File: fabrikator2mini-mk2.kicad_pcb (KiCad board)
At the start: 2 copper layers, 100 x 100 mm, 118 parts, among them CON1 Micro_SD_Card, J1 USB_OTG, J10 END_X/ESP, J11 MT_Y, J12 Conn_01x12, J13 Z, J14 MT_Z, J15 B, J16 BTN1, J17 Fan1, J2 RESET, J3 PWR_IN, J4 B, J5 I2C, J6 SWD, J7 SPI, J8 Fan2, J9 MT_X, P16 SW_DIP, P17 SW_DIP, P18 SW_DIP, P19 SW_DIP, Q1 PSMN2R4-30MLD, Q2 PSMN2R4-30MLD, Q3 PSMN2R4-30MLD, Q4 PSMN2R4-30MLD, Q5 Si7145DP, U1 bluepill, U2 CPDT6-5V4, U3 CPDT6-5V4, U4 4988, U5 4988, U6 4988, U7 4988, U9 TS30011

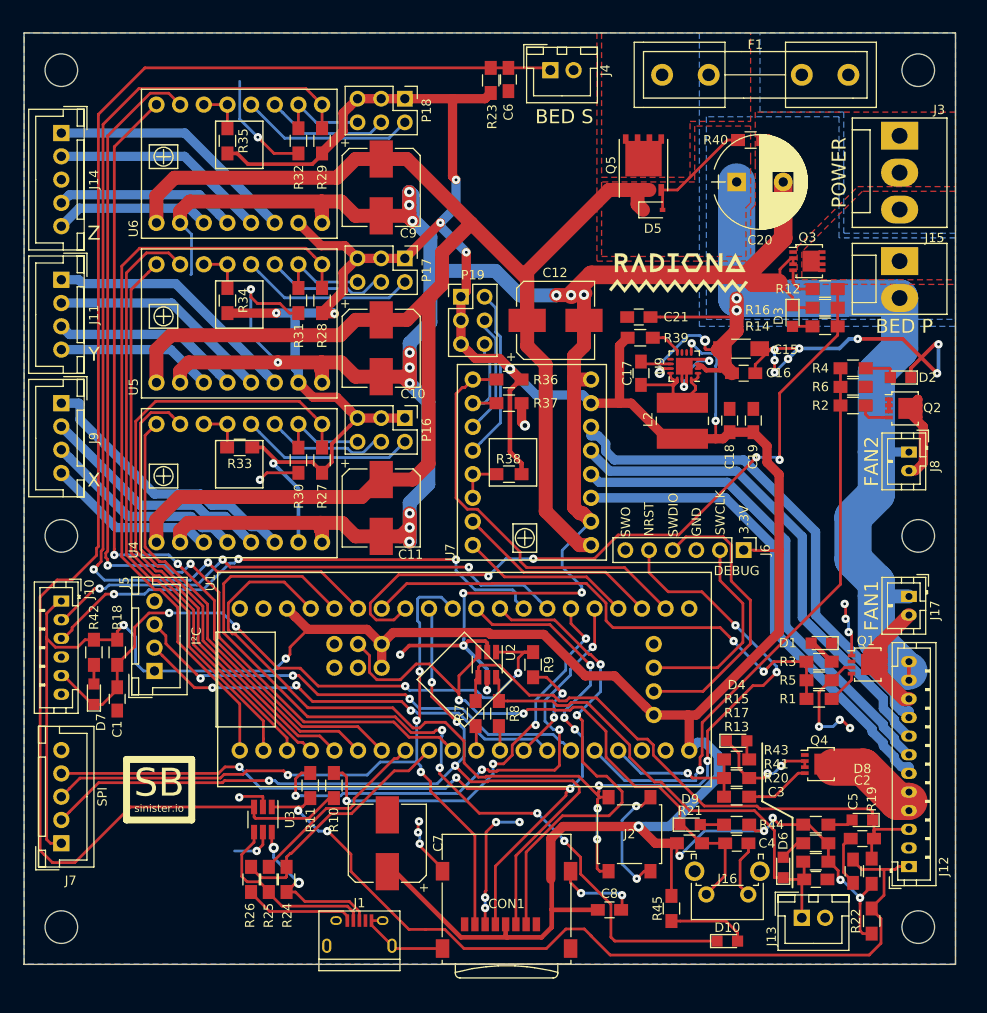
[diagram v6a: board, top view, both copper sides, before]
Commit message: fixed modules after switch to kicad 5
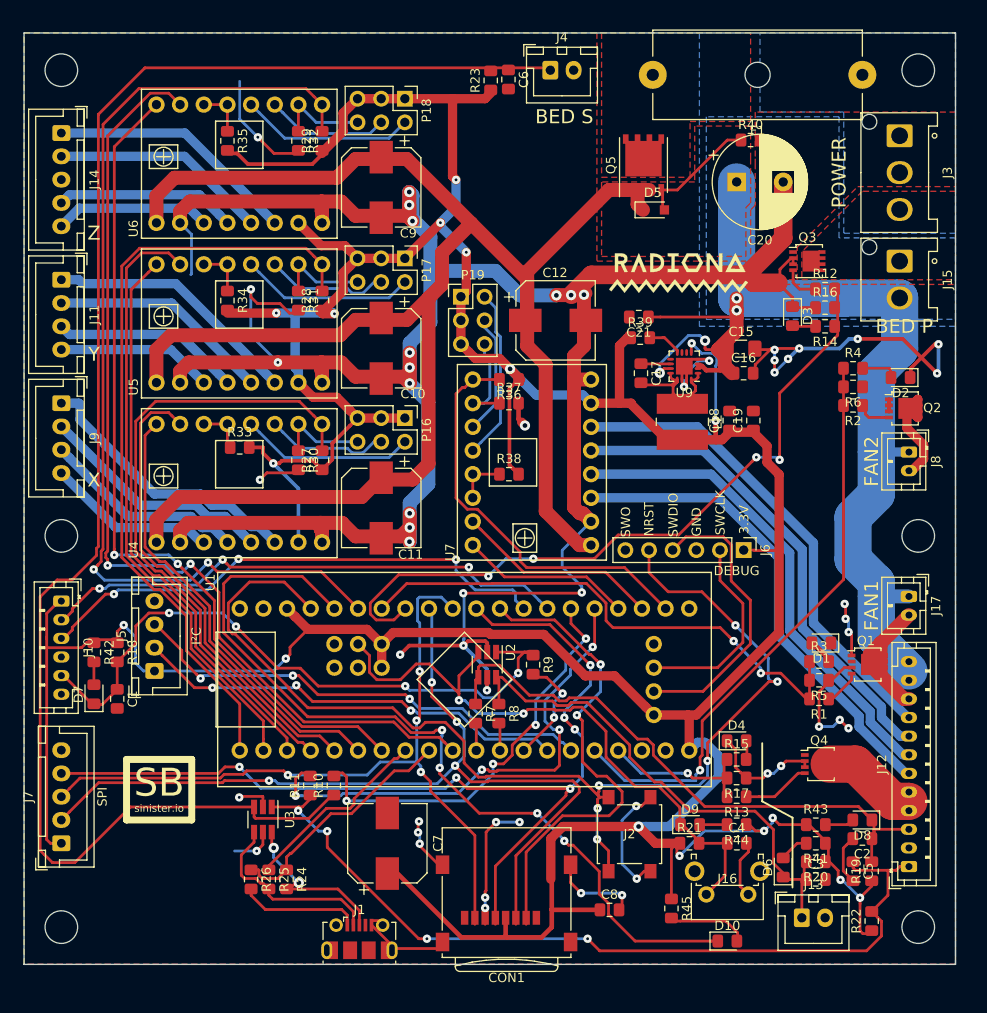
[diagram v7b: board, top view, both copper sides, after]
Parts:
- C1, C16, C17, C18, C19, C2, C21, C3, C4, C5, C6, C8: footprint Capacitors_SMD:C_0805_HandSoldering -> Capacitor_SMD:C_0805_2012Metric_Pad1.15x1.40mm_HandSolder
- C10, C11, C12, C7, C9: footprint Capacitors_SMD:CP_Elec_8x10 -> Capacitor_SMD:CP_Elec_8x10
- C15: footprint Capacitors_SMD:C_1206_HandSoldering -> Capacitor_SMD:C_1206_3216Metric_Pad1.42x1.75mm_HandSolder
- C20: footprint Capacitors_THT:CP_Radial_D10.0mm_P5.00mm -> Capacitor_THT:CP_Radial_D10.0mm_P5.00mm
- CON1: footprint Connectors:microSD_Card_Receptacle_Wuerth_693072010801 -> Connector_Card:microSD_HC_Wuerth_693072010801
- D1, D10, D2, D3, D4, D6, D7, D8, D9: footprint LEDs:LED_0805 -> LED_SMD:LED_0805_2012Metric_Pad1.15x1.40mm_HandSolder
- D5: footprint Diodes_SMD:D_SOD-323 -> Diode_SMD:D_SOD-323_HandSoldering
- F1: footprint Fuse_Holders_and_Fuses:Fuseholder5x20_horiz_open_inline_Type-I -> Fuse:Fuseholder_Cylinder-5x20mm_Schurter_0031_8201_Horizontal_Open
- J1: footprint Connectors:USB_Micro-B -> Connector_USB:USB_Micro-B_Molex-105017-0001
- J10: footprint Connectors_JST:JST_PH_B6B-PH-K_06x2.00mm_Straight -> Connector_JST:JST_PH_B6B-PH-K_1x06_P2.00mm_Vertical
- J11, J5, J9: footprint Connectors_JST:JST_XH_B04B-XH-A_04x2.50mm_Straight -> Connector_JST:JST_XH_B04B-XH-A_1x04_P2.50mm_Vertical
- J12: footprint Connectors_JST:JST_PH_B12B-PH-K_12x2.00mm_Straight -> Connector_JST:JST_PH_B12B-PH-K_1x12_P2.00mm_Vertical
- J13, J4: footprint Connectors_JST:JST_XH_B02B-XH-A_02x2.50mm_Straight -> Connector_JST:JST_XH_B02B-XH-A_1x02_P2.50mm_Vertical
- J14, J7: footprint Connectors_JST:JST_XH_B05B-XH-A_05x2.50mm_Straight -> Connector_JST:JST_XH_B05B-XH-A_1x05_P2.50mm_Vertical
- J15: footprint Connectors_Molex:Molex_KK-41791-02_02x3.96mm_Straight -> Connector_Hirose:Hirose_DF63-2P-3.96DSA_1x02_P3.96mm_Horizontal
- J16: footprint Buttons_Switches_THT:SW_Tactile_SPST_Angled_PTS645Vx58-2LFS -> Button_Switch_THT:SW_Tactile_SPST_Angled_PTS645Vx58-2LFS
- J17, J8: footprint Connectors_JST:JST_PH_B2B-PH-K_02x2.00mm_Straight -> Connector_JST:JST_PH_B2B-PH-K_1x02_P2.00mm_Vertical
- J2: footprint Buttons_Switches_SMD:SW_SPST_B3S-1000 -> Button_Switch_SMD:SW_SPST_B3S-1000
- J3: footprint Connectors_Molex:Molex_KK-41791-03_03x3.96mm_Straight -> Connector_Hirose:Hirose_DF63-3P-3.96DSA_1x03_P3.96mm_Horizontal
- L2: footprint Choke_SMD:Choke_SMD_Wuerth-WE-PD2-Typ-MS -> Inductor_SMD:L_Wuerth_WE-PD2-Typ-MS
- P16, P17, P18, P19: footprint Pin_Headers:Pin_Header_Straight_2x03_Pitch2.54mm -> Connector_PinHeader_2.54mm:PinHeader_2x03_P2.54mm_Vertical
- Q1, Q2, Q3, Q4: footprint TO_SOT_Packages_SMD:LFPAK33 -> Package_TO_SOT_SMD:LFPAK33
- Q5: footprint SMD_Packages:SO-8_PowerPAK_Vishay_Single -> Package_SO:PowerPAK_SO-8_Single
- R1, R10, R11, R12, R13, R14, R15, R16, R17, R18, R19, R2, R20, R21, R22, R23, R24, R25, R26, R27, R28, R29, R3, R30, R31, R32, R33, R34, R35, R36, R37, R38, R39, R4, R40, R41, R42, R43, R44, R45, R5, R6, R7, R8, R9: footprint Resistors_SMD:R_0805_HandSoldering -> Resistor_SMD:R_0805_2012Metric_Pad1.15x1.40mm_HandSolder
- U2, U3: footprint TO_SOT_Packages_SMD:SOT-23-6_Handsoldering -> Package_TO_SOT_SMD:SOT-23-6_Handsoldering
- U9: footprint Housings_DFN_QFN:QFN-16-1EP_3x3mm_Pitch0.5mm -> Package_DFN_QFN:QFN-16-1EP_3x3mm_P0.5mm_EP1.8x1.8mm
- moved F1 1.50 mm to (110.0, 24.5)
- moved J1 0.60 mm to (56.0, 117.2)
- moved CON1 0.45 mm to (71.8, 113.5)
- moved L2 0.11 mm to (90.7, 61.8)
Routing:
- net E_1B: track 54.4 -> 52.1 mm
- net HOTEND_SENSE: track 92.9 -> 91.1 mm, vias 2 -> 4
- net Vsw: track 13.0 -> 14.6 mm
- net VCC: track 321.3 -> 320.1 mm
- net +3V3: track 487.6 -> 488.8 mm
- net FAN1: track 56.2 -> 57.3 mm
- net +5V: track 11.9 -> 13.0 mm
- net LED1: track 92.1 -> 91.2 mm
- net END_Z: track 53.5 -> 54.4 mm
- net USB_D-: track 19.9 -> 20.7 mm
- net USB_D+: track 18.0 -> 18.7 mm
- net E_2B: track 52.6 -> 52.0 mm
- net HOTEND_PWR: track 16.7 -> 17.3 mm
- net END_Y: track 63.5 -> 62.9 mm

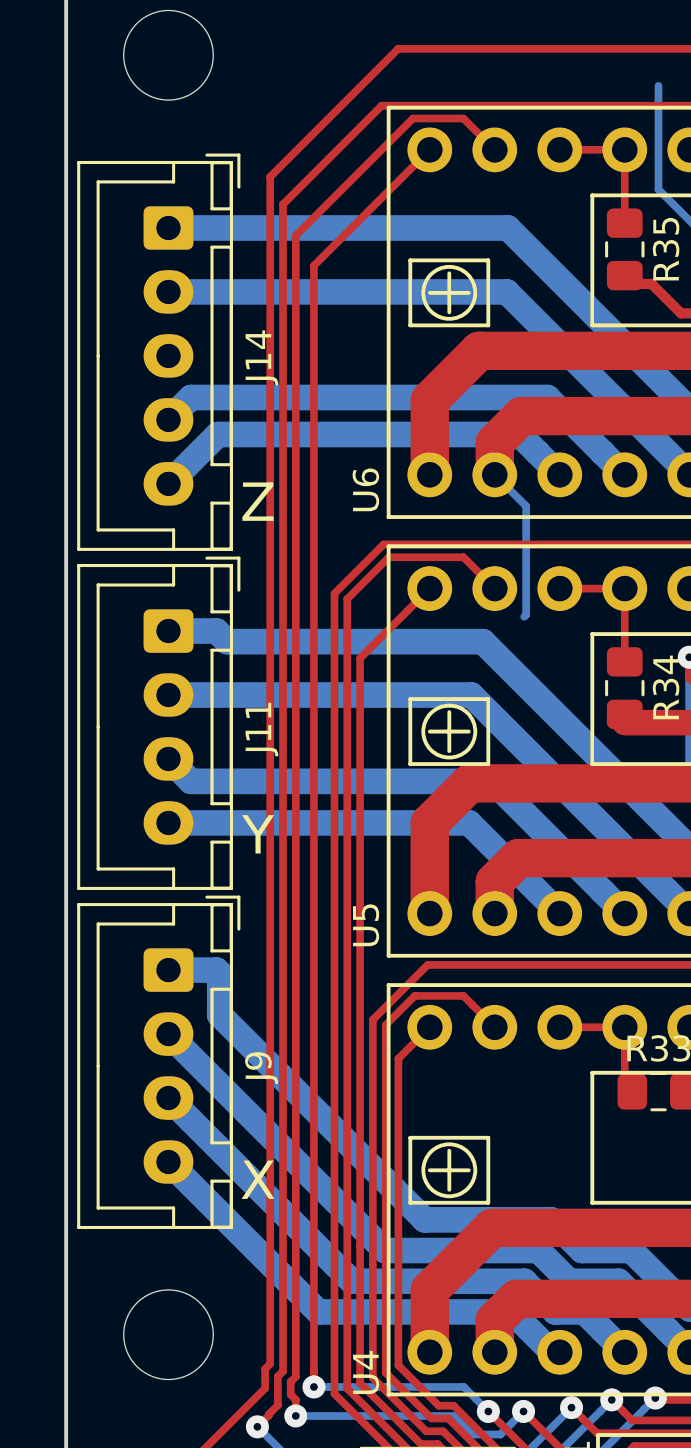
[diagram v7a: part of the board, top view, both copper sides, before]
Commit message: rotated X Y Z connectos to correct orientation
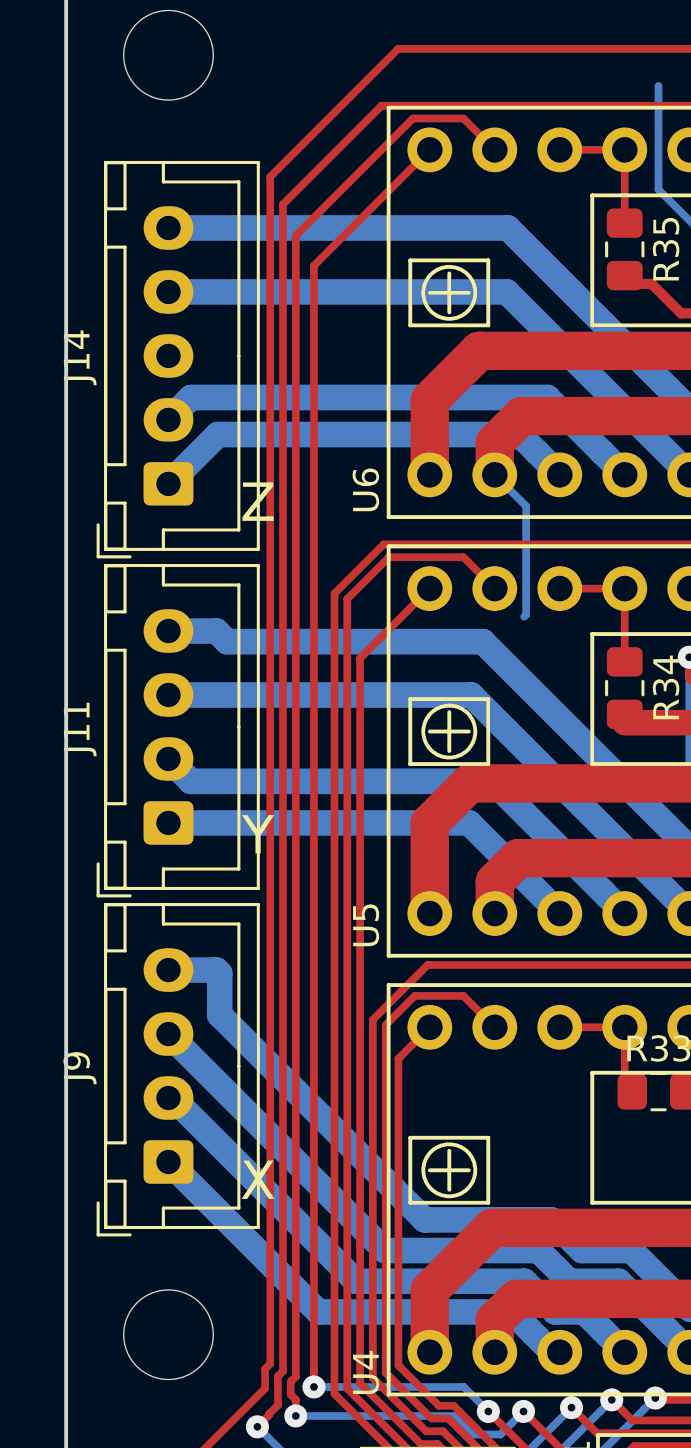
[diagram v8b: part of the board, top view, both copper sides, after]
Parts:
- moved J14 10.0 mm to (24.0, 40.8), turned to 90 degrees
- moved J11 7.50 mm to (24.0, 54.0), turned to 90 degrees
- moved J9 7.50 mm to (24.0, 67.2), turned to 90 degrees
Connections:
- CON1 pad 1: (no net) -> Net-(CON1-Pad1)
- CON1 pad 8: (no net) -> Net-(CON1-Pad8)
- J1 pad 4: (no net) -> Net-(J1-Pad4)
- J11 pad 1: Y_1B -> Y_2B
- J11 pad 2: Y_1A -> Y_2A
- J11 pad 3: Y_2A -> Y_1A
- J11 pad 4: Y_2B -> Y_1B
- J14 pad 1: Z_1B -> Z_2B
- J14 pad 2: Z_1A -> Z_2A
- J14 pad 3: (no net) -> Net-(J14-Pad3)
- J14 pad 4: Z_2A -> Z_1A
- J14 pad 5: Z_2B -> Z_1B
- J6 pad 6: (no net) -> Net-(J6-Pad6)
- J9 pad 1: X_1B -> X_2B
- J9 pad 2: X_1A -> X_2A
- J9 pad 3: X_2A -> X_1A
- J9 pad 4: X_2B -> X_1B
- U1 pad BT0: (no net) -> Net-(U1-PadBT0)
- U1 pad VBAT: (no net) -> Net-(U1-PadVBAT)
- U1 pad VCC: (no net) -> Net-(U1-PadVCC)
- U9 pad 6: (no net) -> Net-(U9-Pad6)
- U9 pad 7: (no net) -> Net-(U9-Pad7)
- U9 pad 9: (no net) -> Net-(U9-Pad9)
